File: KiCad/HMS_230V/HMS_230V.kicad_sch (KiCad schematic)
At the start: 11 parts, among them SW1 SW_SPDT_312, SW2 SW_SPDT_312, U1 Circulator_Gas, U2 Circulator_Wood, U3 Pipe_Thermostat_Gas, U4 Pipe_Thermostat_Wood, U5 Ball_Valve_Gas, U6 Ball_Valve_Wood, U8 MVPDM-1PHS, U9 MVPDM-1PHS

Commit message: Schematic printouts
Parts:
- SW1: value SW_SPDT_312 -> SWITCH_1
- SW2: value SW_SPDT_312 -> SWITCH_2
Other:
- note added: "DIN Power socket"
- note added: "Distribution box"
- note added: "Lever connector terminal blocks"
- note added: "Voltage presence detection modules"
- note removed: "Electrical panel"
- title: (none) -> HMS-230V
- moved on the sheet: SW1, SW2, U1, U2, U3, U4, U5, U6, U7, U8, U9

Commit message: Sensor manager and data manager finalization
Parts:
- removed U7: (no value), symbol HMS_Symbols:Connector_Grounded
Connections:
- net at U4.1 (Low): no longer U8.N
- net at U4.3 (High): no longer U9.N
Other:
- note added: "+"
- note added: "-"
- note added: "ESP32 power supply"
- note removed: "DIN Power socket"

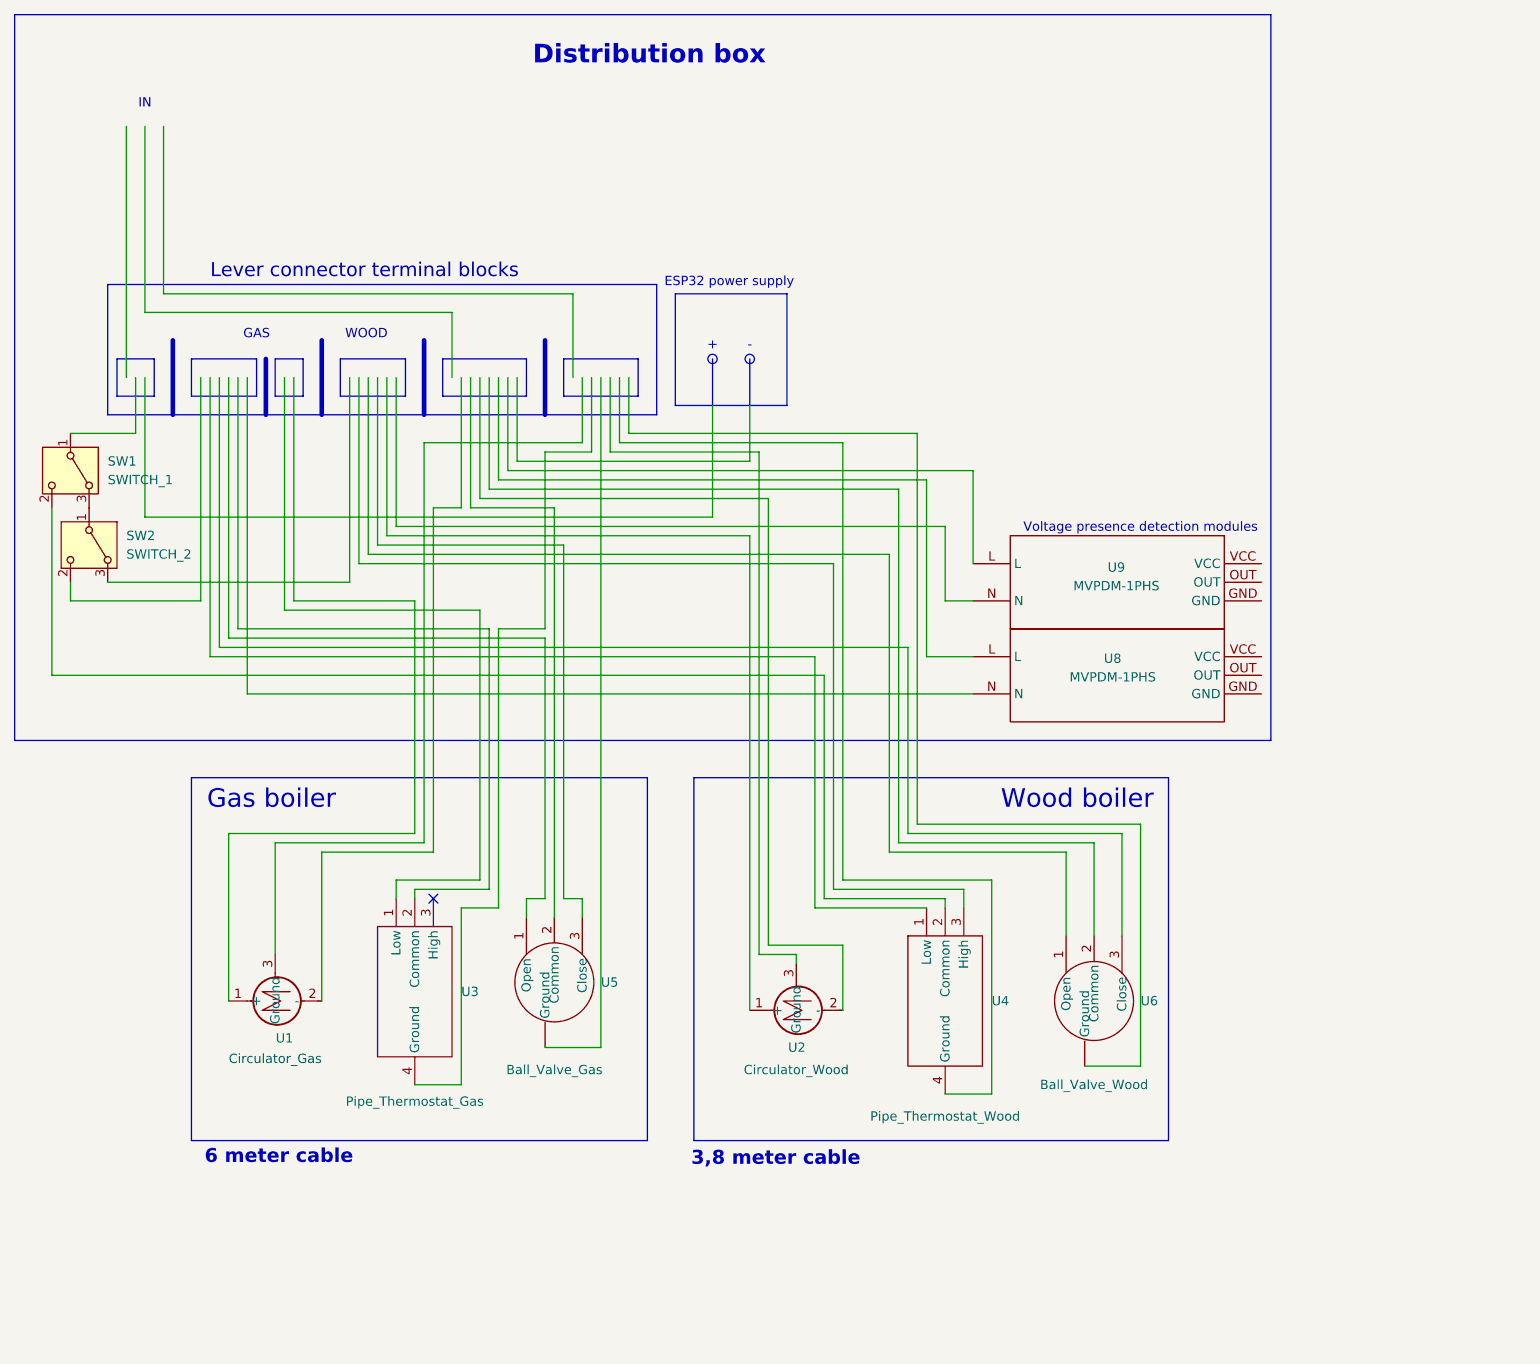
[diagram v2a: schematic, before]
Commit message: 230V connection schematic polishing
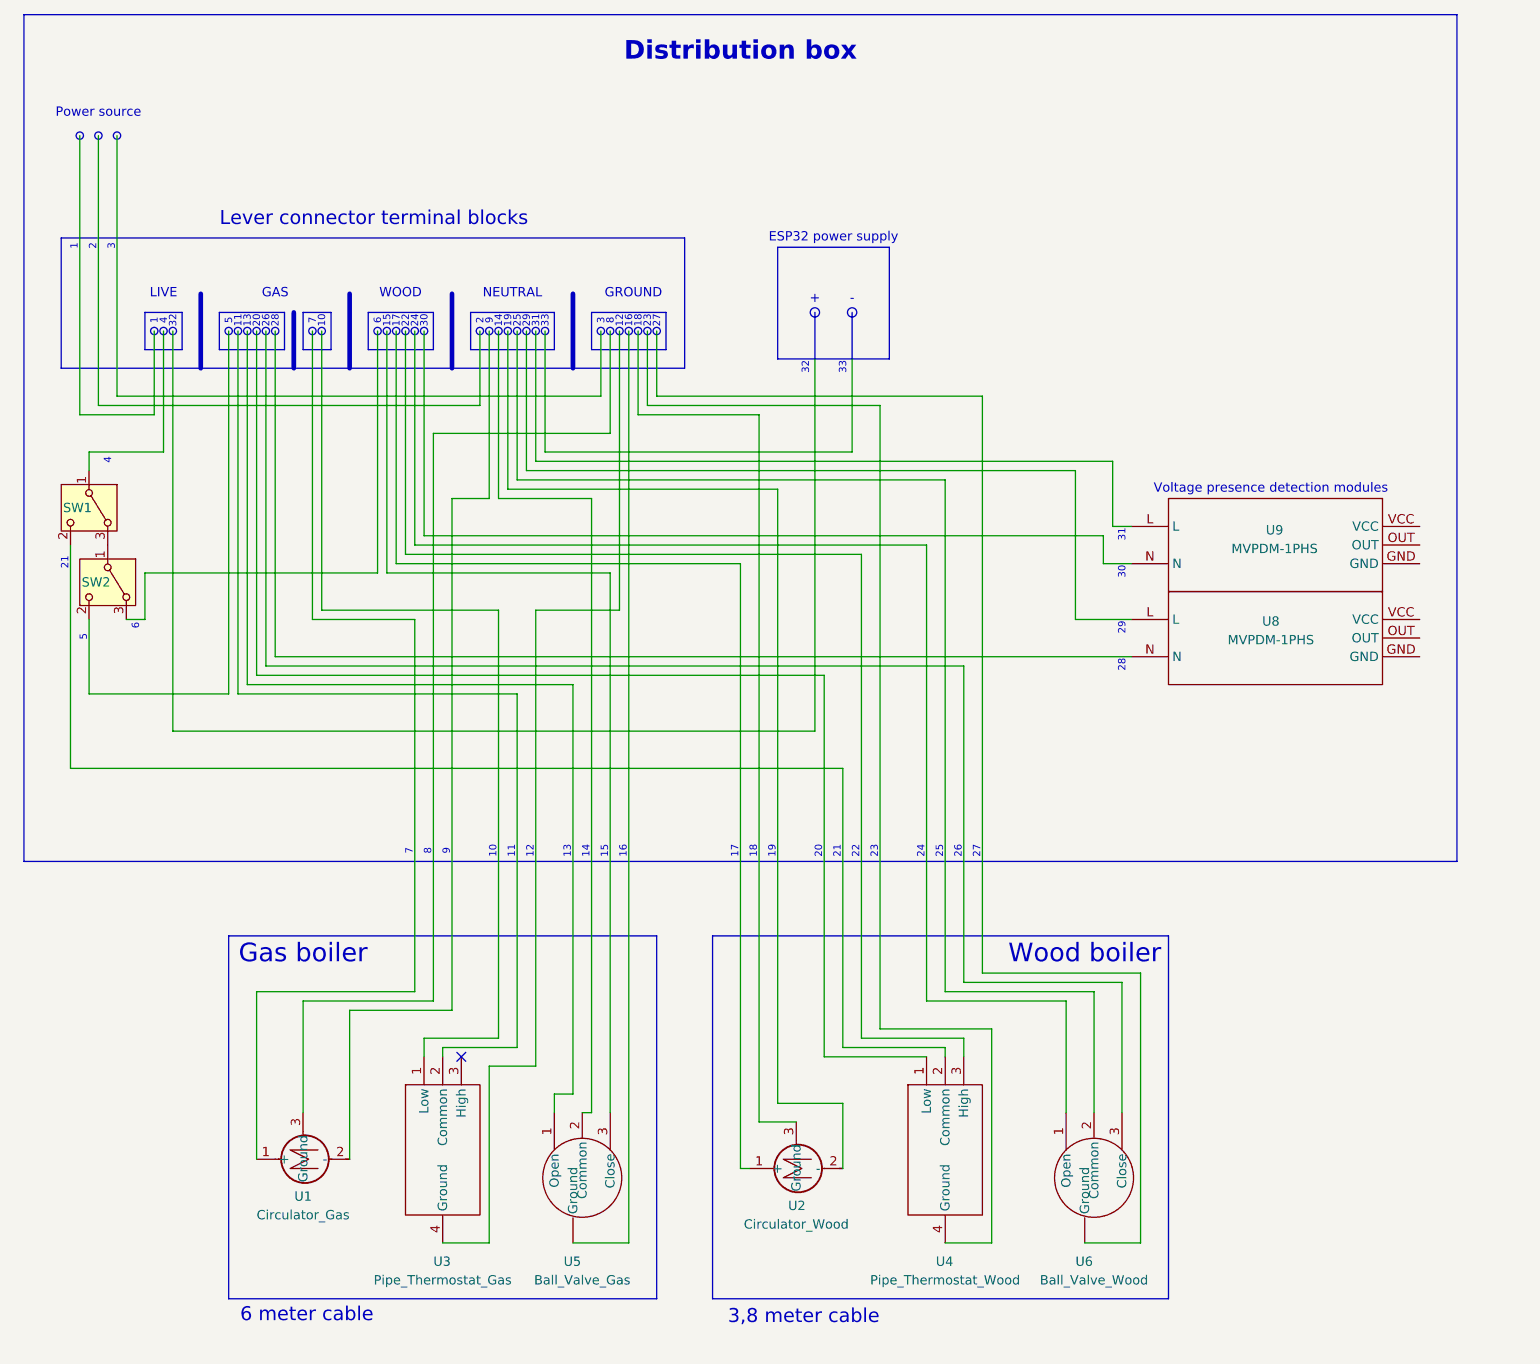
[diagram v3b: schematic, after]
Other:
- note added: "1"
- note added: "10"
- note added: "11"
- note added: "12"
- note added: "13"
- note added: "14"
- note added: "15"
- note added: "16"
- note added: "17"
- note added: "18"
- note added: "19"
- note added: "2"
- note added: "20"
- note added: "21"
- note added: "22"
- note added: "23"
- note added: "24"
- note added: "25"
- note added: "26"
- note added: "27"
- note added: "28"
- note added: "29"
- note added: "3"
- note added: "30"
- note added: "31"
- note added: "32"
- note added: "33"
- note added: "4"
- note added: "5"
- note added: "6"
- note added: "7"
- note added: "8"
- note added: "9"
- note added: "GROUND"
- note added: "LIVE"
- note added: "NEUTRAL"
- note added: "Power source"
- note removed: "IN"
- moved on the sheet: SW1, SW2, U1, U2, U3, U4, U5, U6, U8, U9

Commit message: DS18B20 sensor address fix and HMS_230V sch in progress
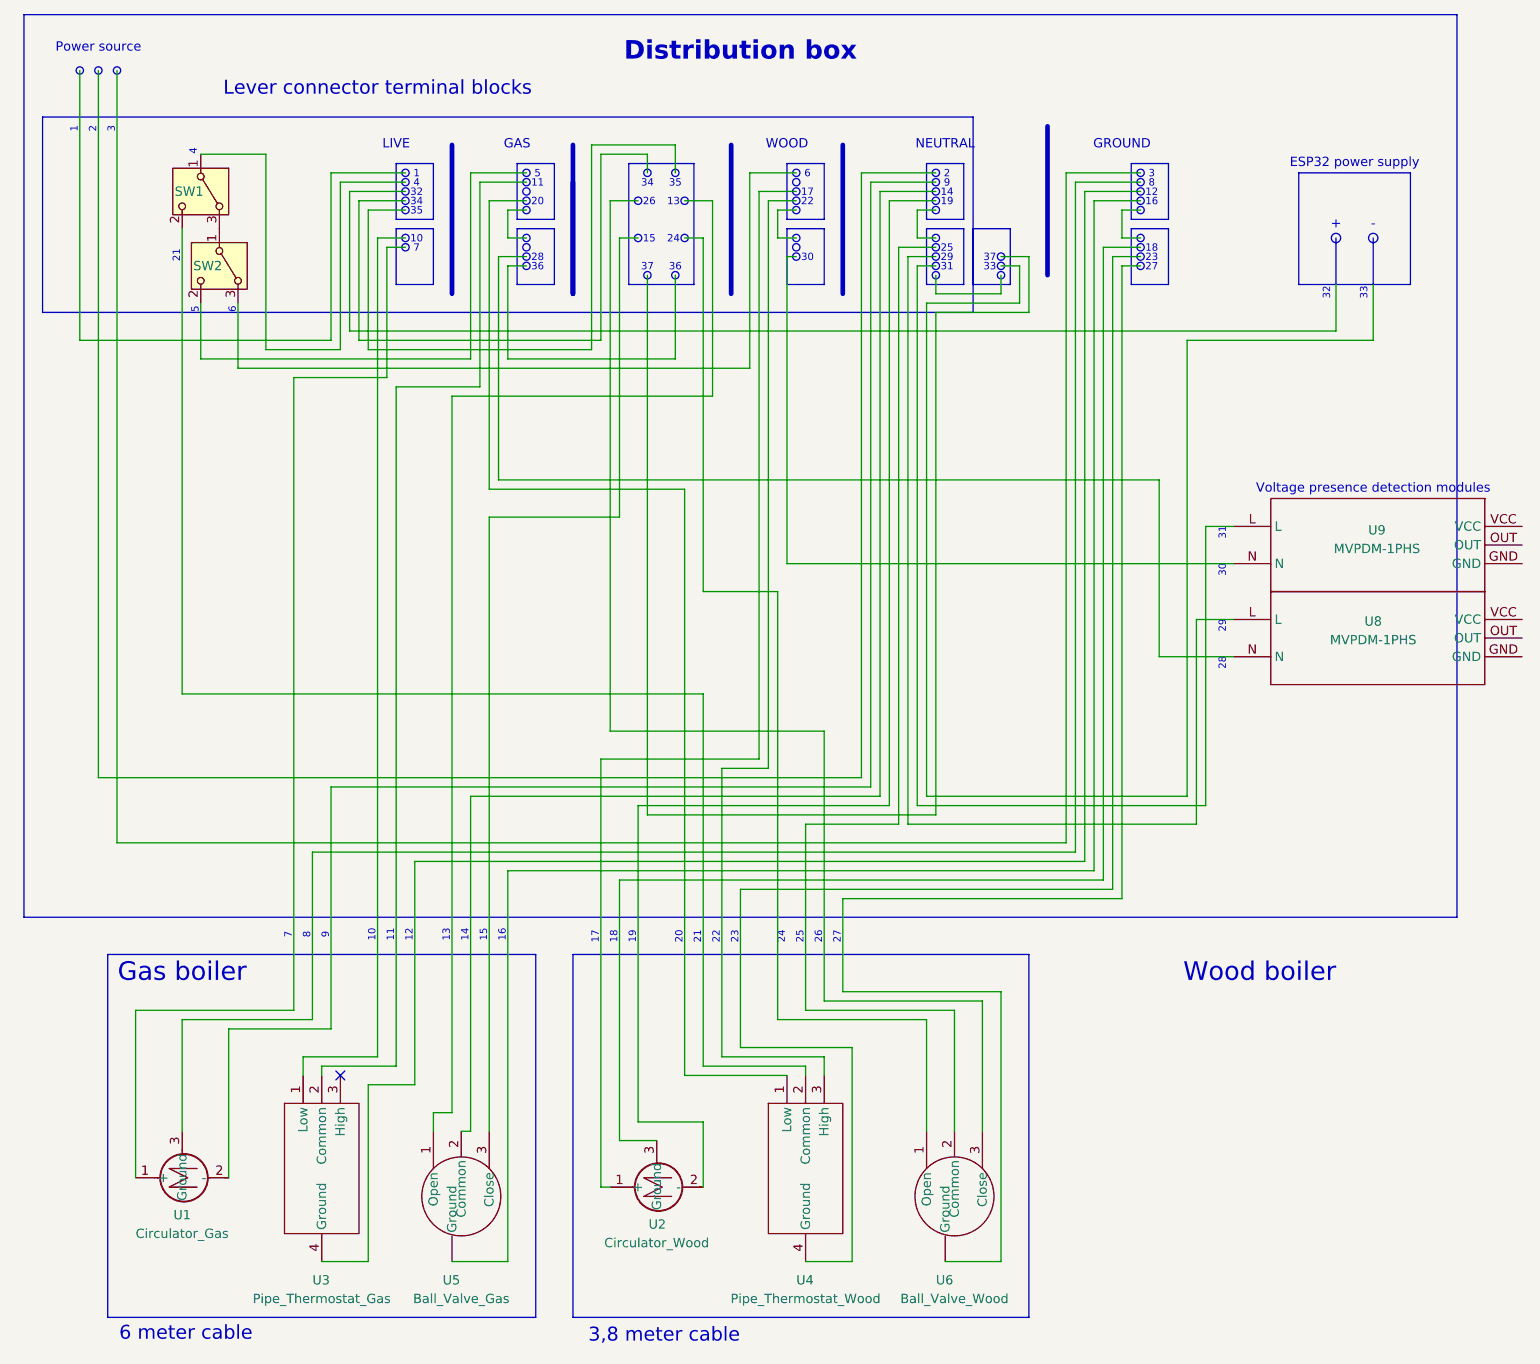
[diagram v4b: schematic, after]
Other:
- note added: "34"
- note added: "35"
- note added: "36"
- note added: "37"
- moved on the sheet: SW1, SW2, U1, U2, U3, U4, U5, U6, U8, U9
